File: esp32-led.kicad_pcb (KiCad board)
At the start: 2 copper layers, 32 parts, among them IC1 ESP32-U4WDH, J1 USB_C_Receptacle_USB2.0, J2 Screw_Terminal_01x02, J3 Screw_Terminal_01x03, J4 JST-PH-4, Q1 MUN5211DW1, SW1 SW_Push, U1 AMS1117-3.3, U2 CP2102N-Axx-xQFN24

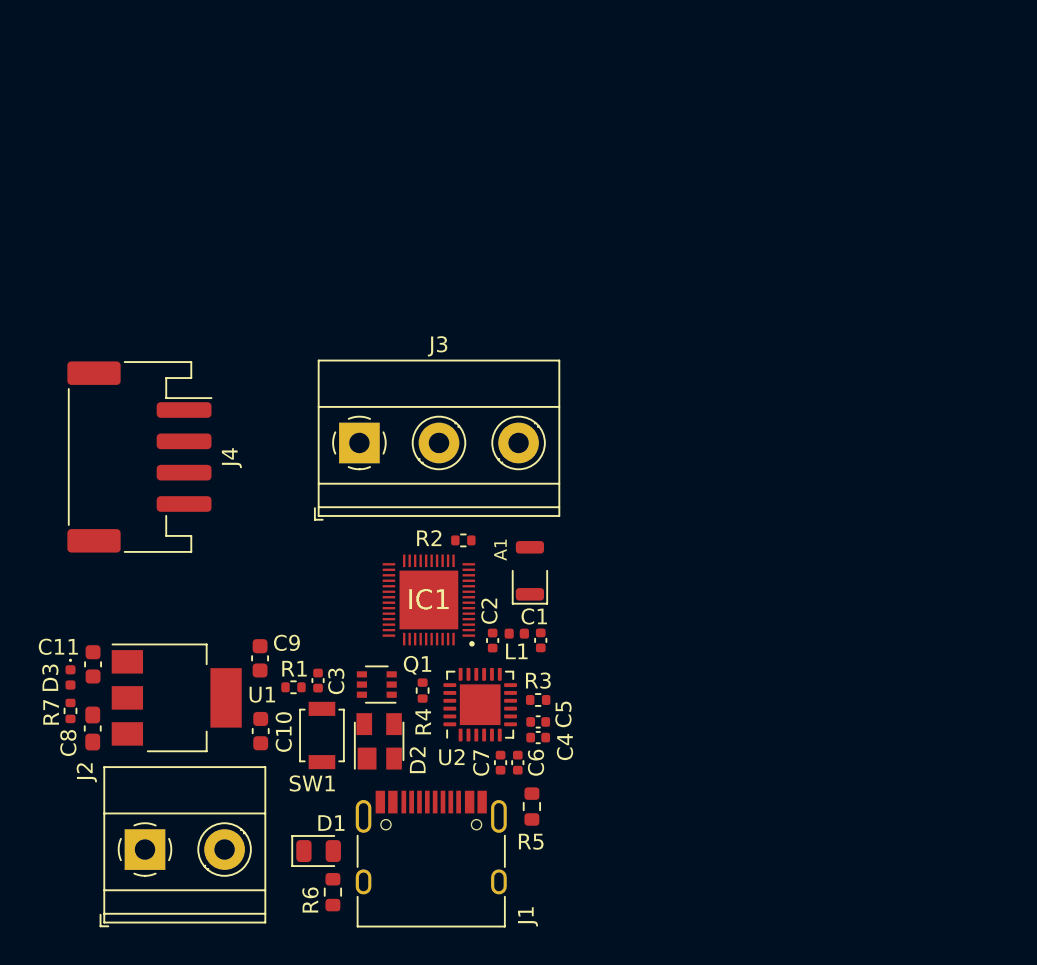
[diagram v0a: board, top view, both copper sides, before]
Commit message: ADD placement and rounting for ESP32-LED Driver
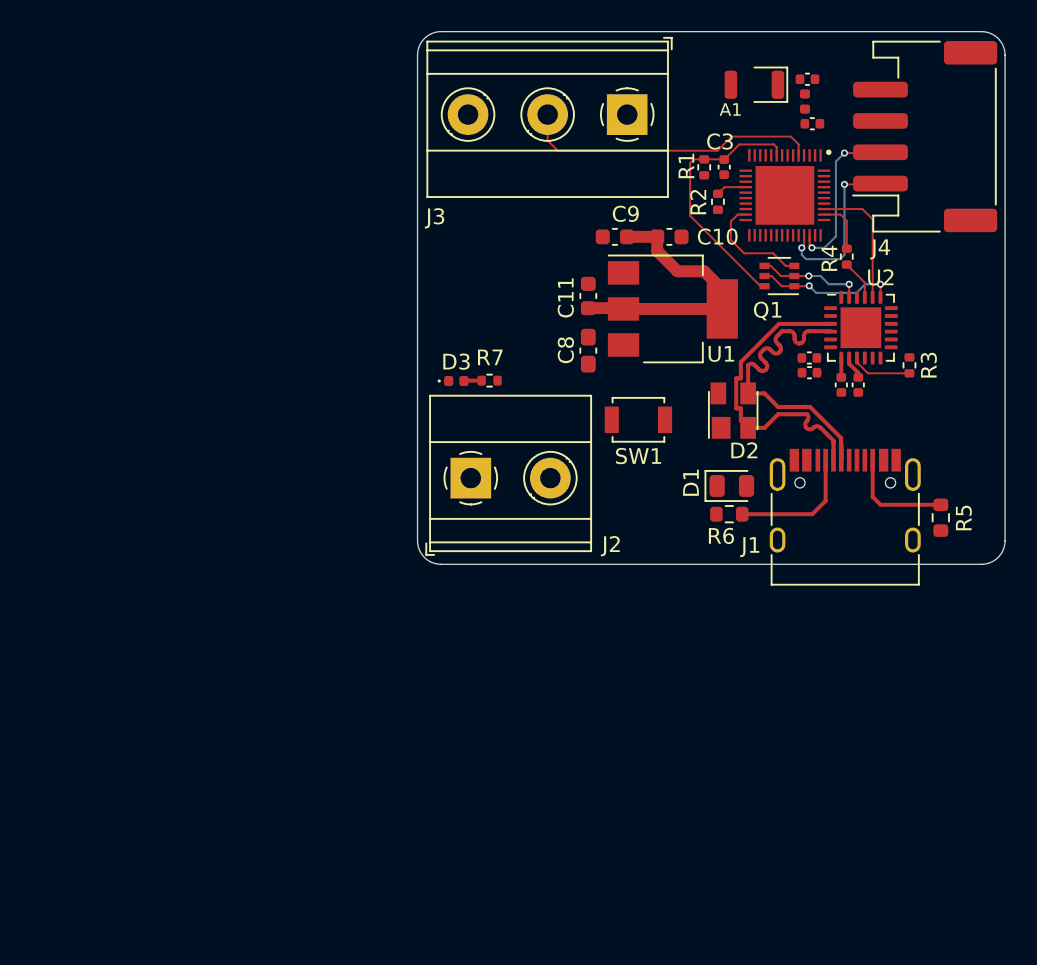
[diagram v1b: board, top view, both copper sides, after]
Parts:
- moved J4 54.2 mm to (150.4, 80.7), turned to 90 degrees
- moved R1 42.3 mm to (136.3, 82.7), turned to 90 degrees
- moved C3 41.8 mm to (137.6, 82.6), turned to -90 degrees
- moved C10 40.9 mm to (134.1, 87.1), turned to 0 degrees
- moved U1 40.2 mm to (134.3, 91.7)
- moved C8 39.8 mm to (128.9, 94.4)
- moved C1 39.7 mm to (142.9, 77.0), turned to 0 degrees
- moved C11 39.4 mm to (128.9, 90.9)
- moved C2 38.8 mm to (143.2, 79.9), turned to 0 degrees
- moved R4 38.7 mm to (145.4, 88.4)
- moved L1 38.6 mm to (142.7, 78.5), turned to -90 degrees
- moved Q1 36.6 mm to (141.1, 89.6)
- moved D1 35.2 mm to (138.1, 103.0)
- moved C9 35.2 mm to (130.6, 87.1), turned to 180 degrees
- moved R6 35.0 mm to (137.9, 104.8), turned to 180 degrees
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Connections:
- D2 pad 2: D- -> D+
- D2 pad 3: D+ -> D-
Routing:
- net D-: track 0.00 -> 20.9 mm
- net +3.3VA: track 0.00 -> 20.5 mm
- net D+: track 0.00 -> 20.2 mm
- net GPIO36: track 0.00 -> 19.2 mm
- net EN: track 0.00 -> 16.6 mm
- net SCL: track 0.00 -> 11.1 mm, vias 0 -> 2
- net SDA: track 0.00 -> 10.6 mm, vias 0 -> 2
- net /USB to UART /RTS: track 0.00 -> 8.93 mm, vias 0 -> 2
- net U0TXD: track 0.00 -> 8.36 mm
- net Net-(J1-PadA5): track 0.00 -> 8.27 mm
- net GPIO0: track 0.00 -> 7.05 mm
- net Net-(J1-PadB5): track 0.00 -> 6.90 mm
- net /USB to UART /DTR: track 0.00 -> 6.72 mm, vias 0 -> 2
- net Net-(R3-Pad2): track 0.00 -> 3.91 mm
- net U0RXD: track 0.00 -> 3.39 mm
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- added copper zone on In2.Cu, net +3.3VA
- added copper zone on In1.Cu, net GND
- added copper zone on In2.Cu, net HIGH_POWER_5V
- added copper zone on In2.Cu, net Net-(D1-Pad2)
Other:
- board outline added: 37.5 x 34 mm
- copper layers 2 -> 4
